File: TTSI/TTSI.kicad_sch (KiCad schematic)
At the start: 28 parts, among them J101 Conn_01x02_Pin, Q101 PMOS, Q102 NMOS, Q103 PMOS, Q104 PMOS, Q105 PMOS, Q106 NMOS, U101 74AHC1G32, U102 LM555xM, U103 74AHC1G08

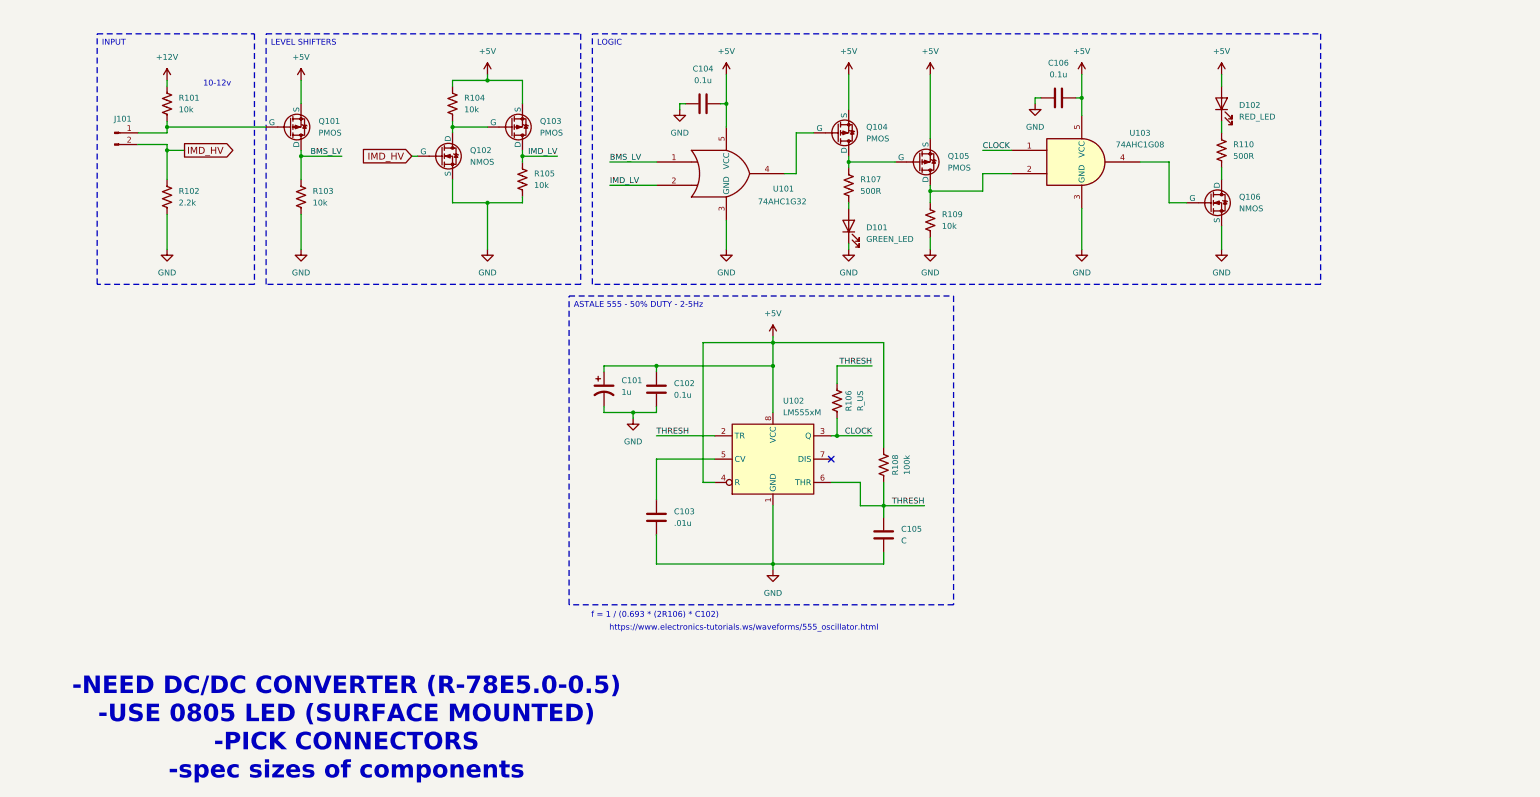
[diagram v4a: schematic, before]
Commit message: Edits to Fault Latch and TSSI
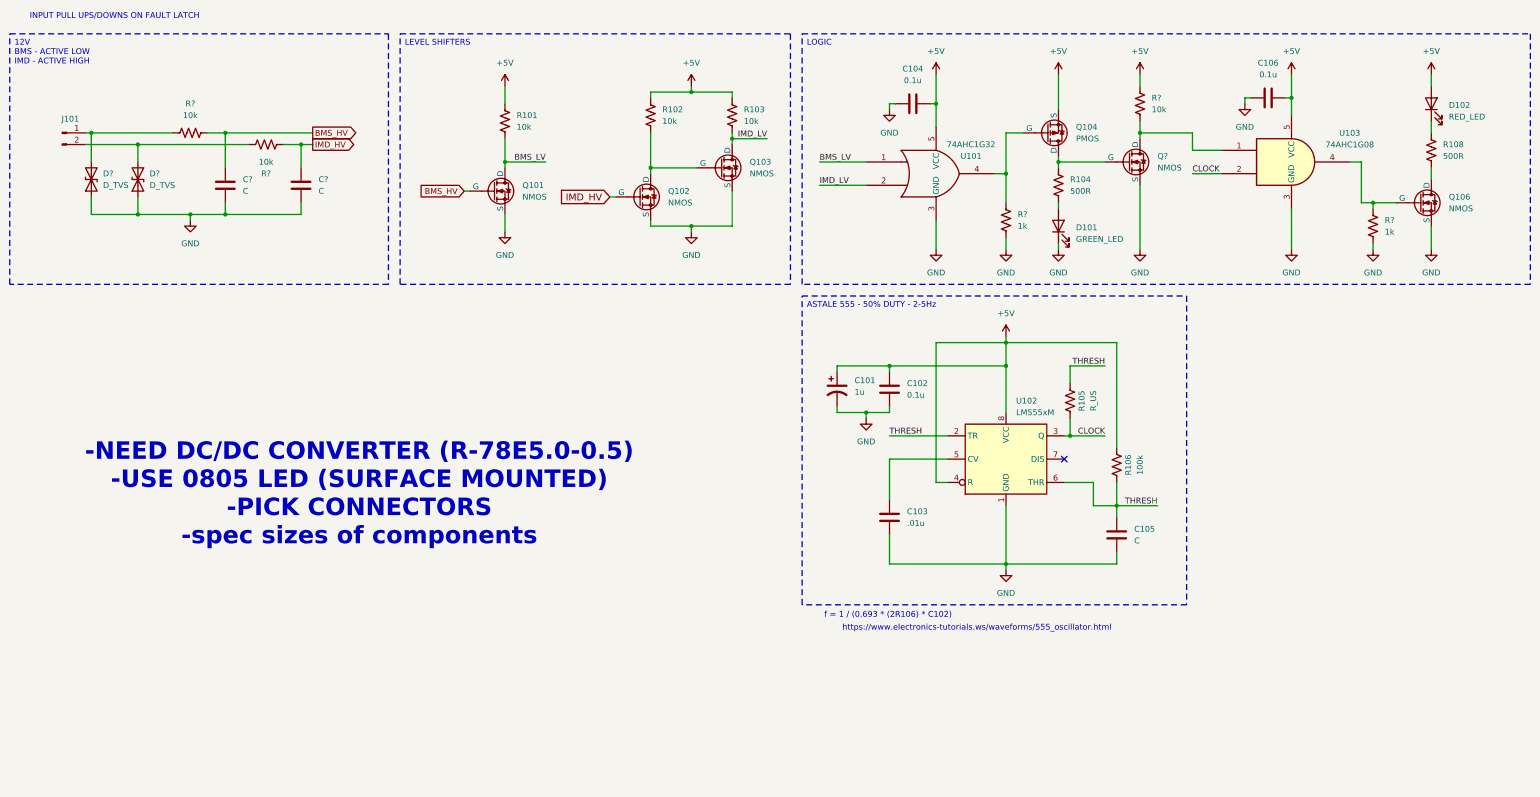
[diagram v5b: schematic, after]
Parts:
- removed Q101, Q103, Q105: PMOS, symbol Simulation_SPICE:PMOS
- removed R101, R105, R109: 10k, symbol Device:R_US
- removed R102: 2.2k, symbol Device:R_US
- added C? (x2): C, Capacitor_SMD:C_0402_1005Metric, symbol Device:C
- added D? (x2): D_TVS, symbol Device:D_TVS
- added Q101, Q103, Q?: NMOS, symbol Simulation_SPICE:NMOS
- added R103, R? (x3): 10k, symbol Device:R_US
- added R? (x2): 1k, symbol Device:R_US
- renumbered R103 to R101, R104 to R102, R107 to R104, R106 to R105, R108 to R106, R110 to R108
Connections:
- net +5V: now also R101.1, R103.1, R?.1
- net BMS_LV: now also R101.2, Q101.1 (D); no longer R101.1
- net CLOCK: now also U103.2; no longer U103.1
- net GND: now also C?.1, C?.1, D?.1 (A1), D?.1 (A1), Q101.3 (S), Q103.3 (S), Q?.3 (S), R?.2, R?.2; no longer R101.2
- net IMD_HV: now also C?.2, R?.1; no longer J101.2 (Pin_2)
- net IMD_LV: now also Q103.1 (D), R103.2
- net at J101.1 (Pin_1): now also D?.2 (A2), R?.1
- net at Q106.2 (G), U103.4: now also R?.1
- net at Q102.1 (D), R102.2: now also Q103.2 (G)
- net at Q104.2 (G), U101.4: now also R?.1
- net at Q104.1 (D), R104.1: now also Q?.2 (G)
- new net: Q?.1 (D), R?.2, U103.1
- new net: D?.2 (A2), J101.2 (Pin_2), R?.2
- new net BMS_HV: C?.2, Q101.2 (G), R?.2
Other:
- note added: "INPUT PULL UPS/DOWNS ON FAULT LATCH"
- note removed: "10-12v"
- moved on the sheet: C101, C102, C103, C104, C105, C106, D101, D102, J101, Q102, Q104, Q106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

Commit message: TSSI Update
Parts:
- removed C? (x2): C, Capacitor_SMD:C_0402_1005Metric, symbol Device:C
- removed D101: GREEN_LED, symbol Device:LED
- removed D102: RED_LED, symbol Device:LED
- removed R108: 500R, symbol Device:R_US
- removed R? (x2): 10k, symbol Device:R_US
- removed R?: 1k, symbol Device:R_US
- added C1, C2: 10uF, Capacitor_SMD:C_0402_1005Metric, symbol Device:C
- added R1: 1k, symbol Device:R_US
- added R2: 500R, symbol Device:R_US
- added U1, U2, U3, U5: 641964-1, 641964-1_TYC, symbol CONNECTOR:641964-1
- added U4: R-78E5.0-0.5, Converter_DCDC:Converter_DCDC_RECOM_R-78E-0.5_THT, symbol Regulator_Switching:R-78E5.0-0.5
- C101: JLC# (none) -> C59782
- C102, C104, C106: JLC# (none) -> C133086
- C103: JLC# (none) -> C15195
- D? (x2): JLC# (none) -> C698991
- Q101, Q102, Q103, Q106, Q?: JLC# (none) -> C151421
- Q104: JLC# (none) -> C96676
- R101, R102, R103, R?: JLC# (none) -> C130232
- R106: JLC# (none) -> C60491
- R?: JLC# (none) -> C105637
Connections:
- net +5V: now also C2.1, R2.1, U4.3 (OUT)
- net BMS_HV: now also D?.2 (A2), J101.1 (Pin_1)
- net GND: now also C1.2, C2.2, R1.2, U1.2, U2.2, U3.2, U4.2 (GND)
- net IMD_HV: now also D?.2 (A2), J101.2 (Pin_2)
- net at Q106.2 (G), U103.4: now also R1.1
- net at Q106.1 (D): now also U5.2
- net at R104.2: now also U3.1
- new net: R2.2, U5.1
- new net +12V: C1.1, U4.1 (IN)
- new net BMS CN: U1.1
- new net IMD CN: U2.1
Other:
- note added: "-NEED DC/DC CONVERTER (R-78E5.0-0.5)(DONE) -PICK CONNECTORS (DONE) -spec sizes of components"
- note added: "0 - 352.8 V"
- note added: "12-5v Converter"
- note added: "All 5v sources above come from this converter"
- note added: "Connectors"
- note added: "Ok these level shifters are shifting these voltages to 5v for the OR GATE logic seen in the logic box"
- note removed: "-NEED DC/DC CONVERTER (R-78E5.0-0.5) -USE 0805 LED (SURFACE MOUNTED) -PICK CONNECTORS -spec sizes of components"
- moved on the sheet: C101, C102, C103, C105, D?, Q106, R105, R106, U102

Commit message: TSSI and FL fixes
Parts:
- removed R104, R2: 500R, symbol Device:R_US
- added D103: RED, symbol Device:LED
- D101, D102: renamed from D?; footprint (none) -> Diode_SMD:D_SOD-123F; JLC# C698991 -> C110748
- R102: value 10k -> 500R
- U107: renamed from U102; JLC# (none) -> C90760
- gave numbers to parts that had none: 3
- renumbered C1 to C101, C2 to C102, C104 to C103, C101 to C104, C102 to C105, C103 to C106, C106 to C107, C105 to C108, R1 to R106, R105 to R107, R106 to R108, U1 to U101, U2 to U102, U4 to U103, U101 to U104, U3 to U105, U103 to U106, U5 to U108
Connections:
- net BMS CN is gone; now on net BMS_HV: U101.1
- net IMD CN is gone; now on net +12V: U102.1
- net +5V: now also U108.1
- net GND: no longer U101.2
- net IMD_HV: now also U101.2
- net at Q102.1 (D), Q103.2 (G): now also D103.1 (K); no longer R102.2
- net at Q104.1 (D), Q105.2 (G): now also U105.1
- new net: D103.2 (A), R102.2
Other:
- note added: "Power/Signal Input Connectors"
- note removed: "-NEED DC/DC CONVERTER (R-78E5.0-0.5)(DONE) -PICK CONNECTORS (DONE) -spec sizes of components"
- note removed: "Connectors"
- moved on the sheet: C101, C102, C103, C104, C105, C106, C107, C108, D101, D102, J101, Q101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
